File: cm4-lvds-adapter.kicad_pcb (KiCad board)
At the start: 6 copper layers, 52 x 43 mm, 155 parts, among them J1 Plug_Molex_SlimStack_2x20_556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, J2 JST_SUR_1x10_SM10B-SURS-TF-LF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, J3 FFC_Amphenol_1x40_62684-40110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, Q1 PJE138K, Q2 PJE138K, Q3 SSM3J332R, Q4 PJE138K, Q5 SSM3J332R, Q6 PJE138K, Q7 SSM3J332R, Q8 PJE138K, U1 TLV70018_SC70, U2 NTS0104_DHVQFN, U3 SN65DSI84, U4 TPS65150_HTSSOP, U5 MPQ7235GQBE, U6 TLV76701_WSON

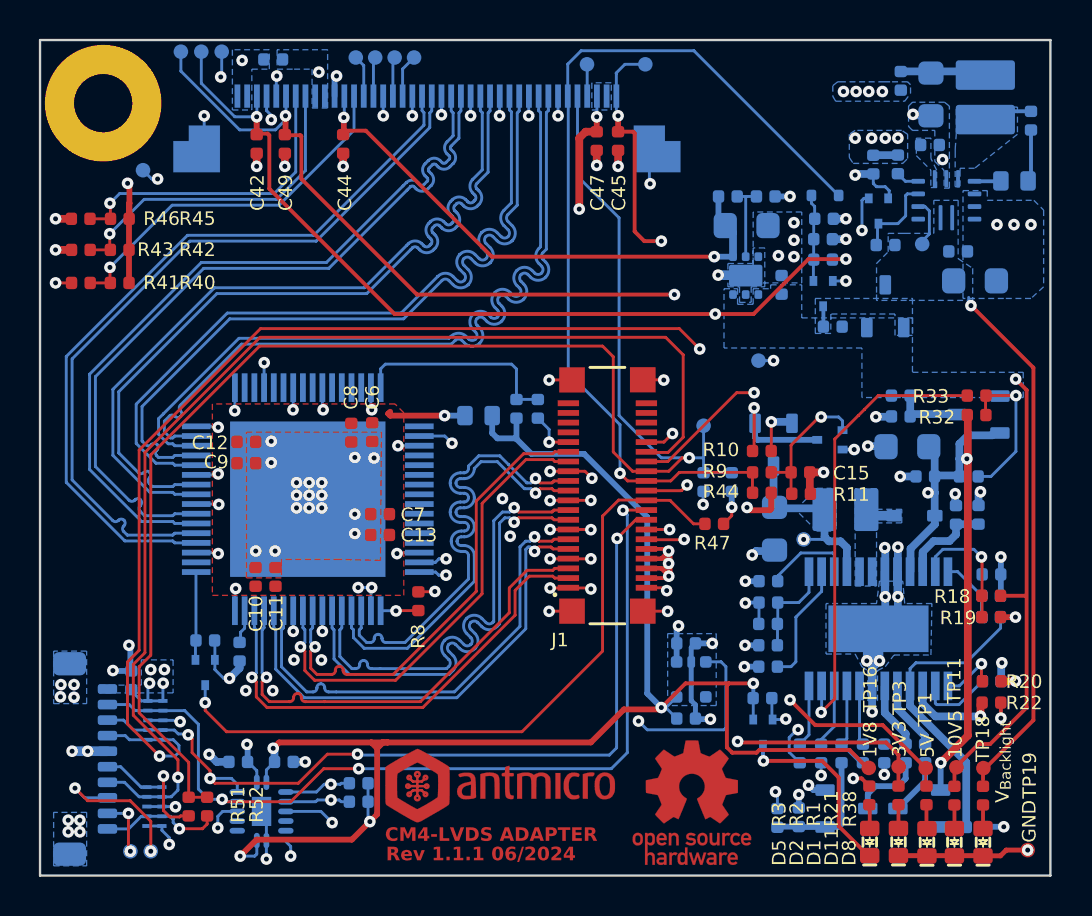
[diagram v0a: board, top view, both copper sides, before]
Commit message: [#62756] Fix R5, synchronize components with library, bumped revision to 1.1.2
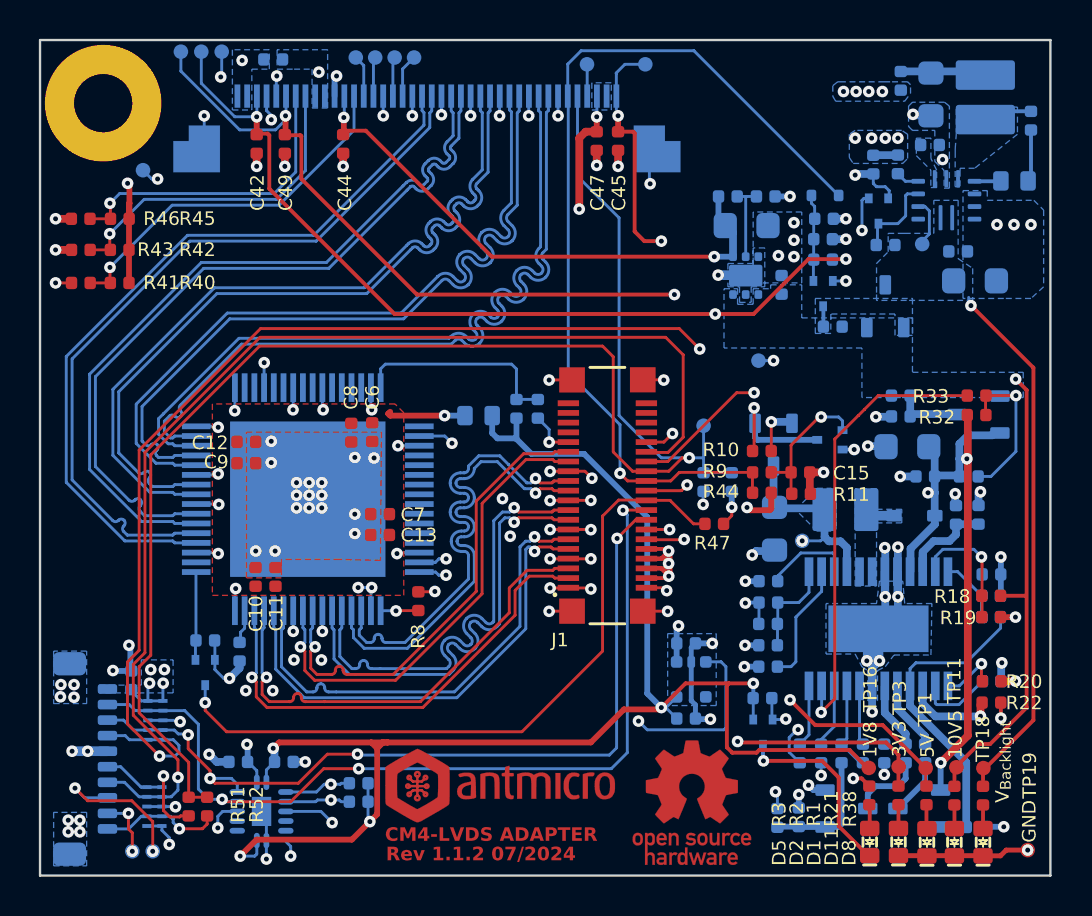
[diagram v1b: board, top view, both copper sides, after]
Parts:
- R5: value C_100n_0402 -> R_0R_0402
- moved TP20 0.11 mm to (147.2, 205.8)
- moved TP6 0.10 mm to (113.8, 221.8)
- moved TP7 0.10 mm to (112.8, 221.8)
- turned R5 to 90 degrees
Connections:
- R5 pad 1: /Power/FDLY -> /Power/Vi_{BOOST}
- R5 pad 2: /Power/Vi_{BOOST} -> /Power/FDLY
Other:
- board text added: "Rev ${REVISION} 07/2024"
- board text removed: "Rev ${REVISION} 06/2024"
